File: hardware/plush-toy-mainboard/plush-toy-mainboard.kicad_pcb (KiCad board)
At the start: 4 copper layers, 90 x 60 mm, 108 parts, among them U1 ESP32-S3-WROOM-1-N16R8

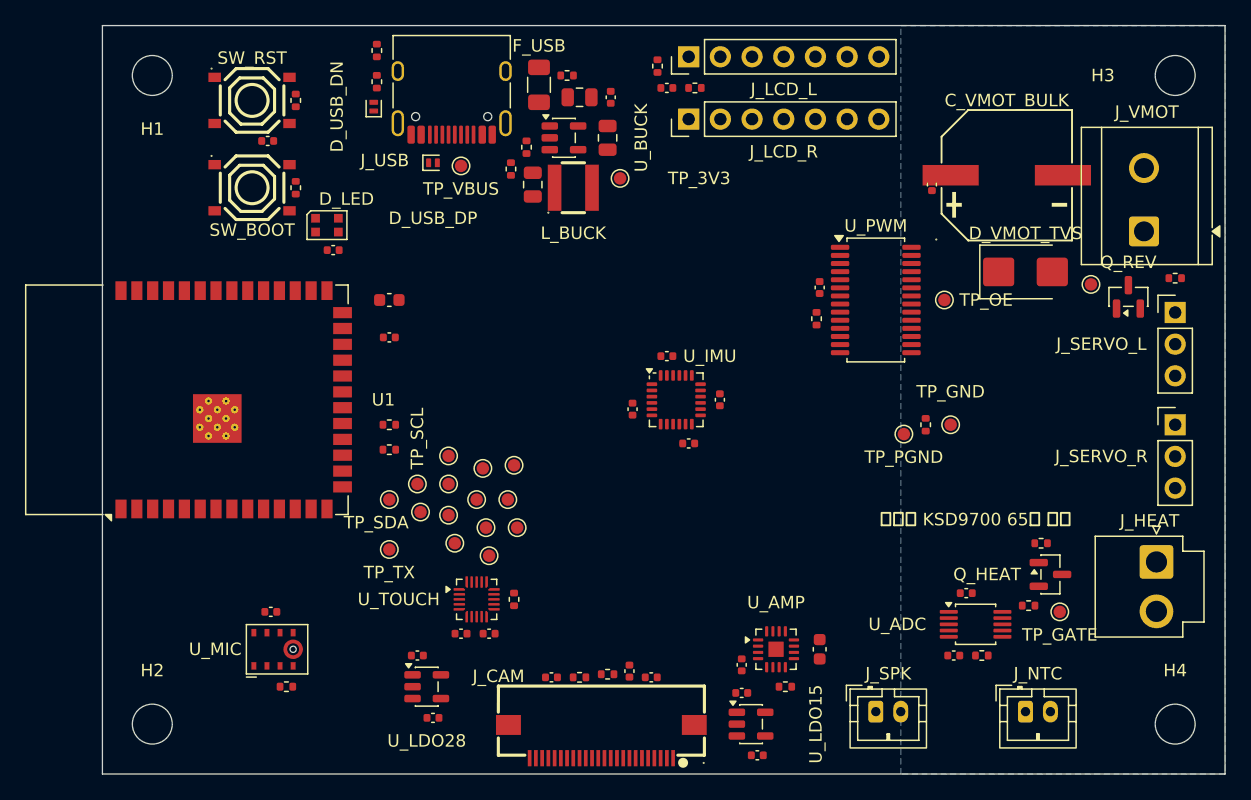
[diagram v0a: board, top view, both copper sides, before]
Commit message: fix(pcb): 布线前 DRC 清零：焊盘短路、铺铜规则、声孔间距
主板实施计划 Task 6 前半。布线前 DRC 零违规，仅剩 251 条待布线连接。

- 焊盘短路：第三方电解电容封装庭院层（±5.2mm）比焊盘（±6.75mm）小，
  自动排布把 C_VMOT_HF 的 PGND 焊盘压在 C_VMOT_BULK 的 VMOT 焊盘上。
  占位改为庭院层 ∪ 焊盘；新增 test_pads_of_different_parts_do_not_touch
- 工程规则：project_rules.py 写入网络类（Default 0.2mm、Supply 0.5mm、
  Power 1.0mm）与最小规则（线宽/间距 0.127、钻孔 0.2、距板边 0.3）
- 铺铜：临时板无工程文件，按默认规则灌铜导致 15 处孔间距、3 处板边间距违规。
  改为加载正式工程后再灌铜
- 板文件安全：生成先写临时文件再替换；此前一次报错清空了正式板文件
- INMP441 声孔 0.5 改 0.4mm：原孔到铜环 0.23mm 低于规则 0.25mm，
  0.4 仍远大于数据手册下限 0.25mm
- 新增 route.py（DSN → Freerouting → SES）与 test_drc.py

Co-Authored-By: Claude Opus 5 <noreply@anthropic.com>
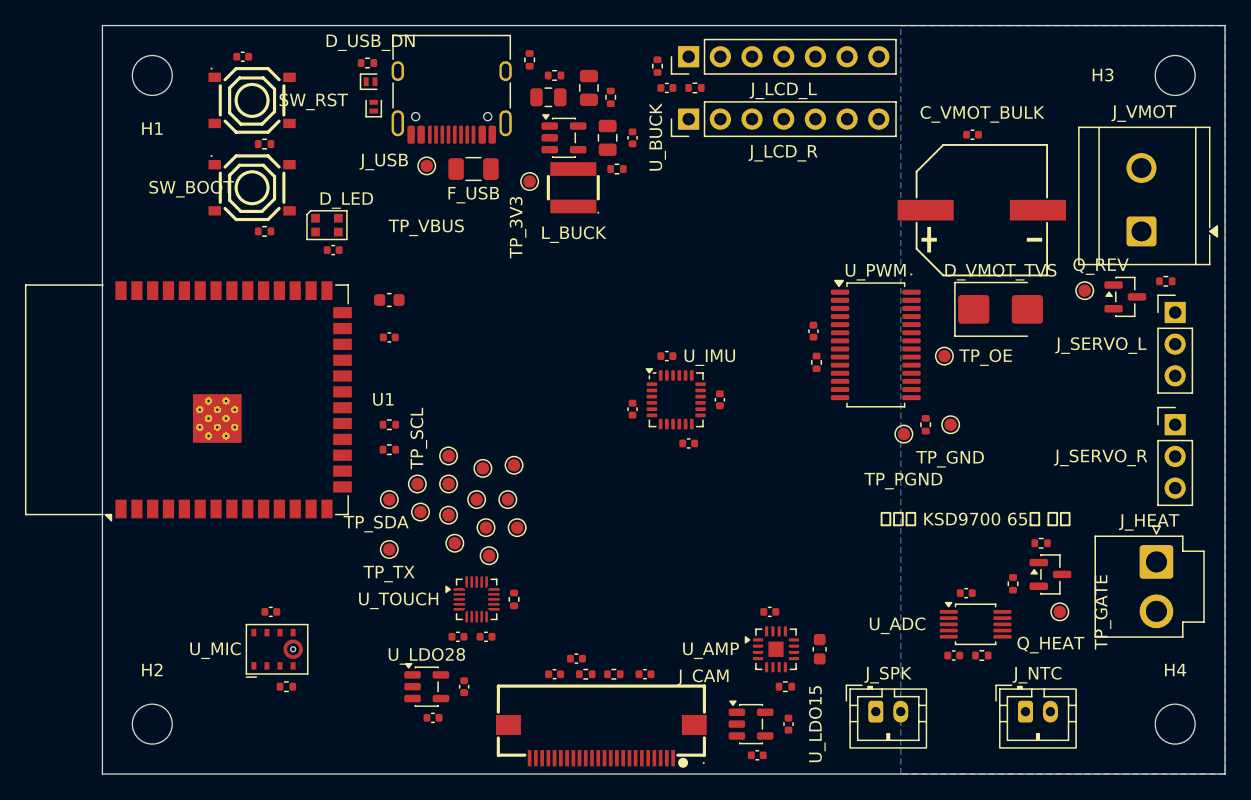
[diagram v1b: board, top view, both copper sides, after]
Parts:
- moved R_CC1 12.4 mm to (34.2, 2.75)
- moved C_BUCK_OUT2 8.96 mm to (39.0, 5.00)
- moved F_USB 8.55 mm to (29.8, 11.5), turned to 0 degrees
- moved R_FB1 8.28 mm to (36.2, 4.00), turned to 0 degrees
- moved C_CAM_AVDD 7.50 mm to (43.5, 52.0)
- moved R_BUCK_EN 7.46 mm to (41.2, 11.5), turned to 0 degrees
- moved TP_3V3 7.25 mm to (34.2, 12.5)
- moved C_EN 7.04 mm to (11.2, 2.50)
- moved D_USB_DP 6.54 mm to (21.8, 6.50), turned to 90 degrees
- moved C_CAM_DVDD 6.18 mm to (38.0, 50.8)
- moved C_CAM_RST 6.01 mm to (36.2, 52.0), turned to 0 degrees
- moved C_VMOT_HF 5.15 mm to (69.8, 8.75), turned to 0 degrees
- moved C_AMP 4.81 mm to (53.5, 47.0), turned to 0 degrees
- moved C_LDO15_OUT 4.51 mm to (55.0, 56.0), turned to 90 degrees
- moved C_LDO28_OUT 4.51 mm to (29.0, 53.0), turned to 90 degrees
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
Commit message: wip(pcb): 自动布线存档——平面扇出 + Freerouting，剩 10 条未连接
主板实施计划 Task 6 进行中，委托方要求在此存档。

- 内层 In1/In2 设为 power 类型：首次布线把 MIC、I2S 线走在了 GND/3V3 平面上
- gen_pcb / route 保存后重写工程规则：board.Save 会用默认规则冲掉 .kicad_pro，
  导致 DRC 按 0.2mm 间距报 370 处假违规
- fanout.py：GND/+3V3 贴片焊盘就近打过孔下平面（101 个），散热焊盘内打孔，
  细间距引脚按 0.15mm 规则间距外扩
- 新增测试：内层无走线、内层为 power 类型、平面网络焊盘均已扇出
- export_fab.sh：Gerber/钻孔/BOM/坐标导出，参数已对照 kicad-cli 10.0.6 帮助核对

当前结果：test_pcb 16 项全绿，与原理图一致；DRC 剩 10 条未连接、
4 处路由器过孔离 U_MIC 声孔过近（0.13mm < 0.25mm）。剩余问题清单见 README。

Co-Authored-By: Claude Opus 5 <noreply@anthropic.com>
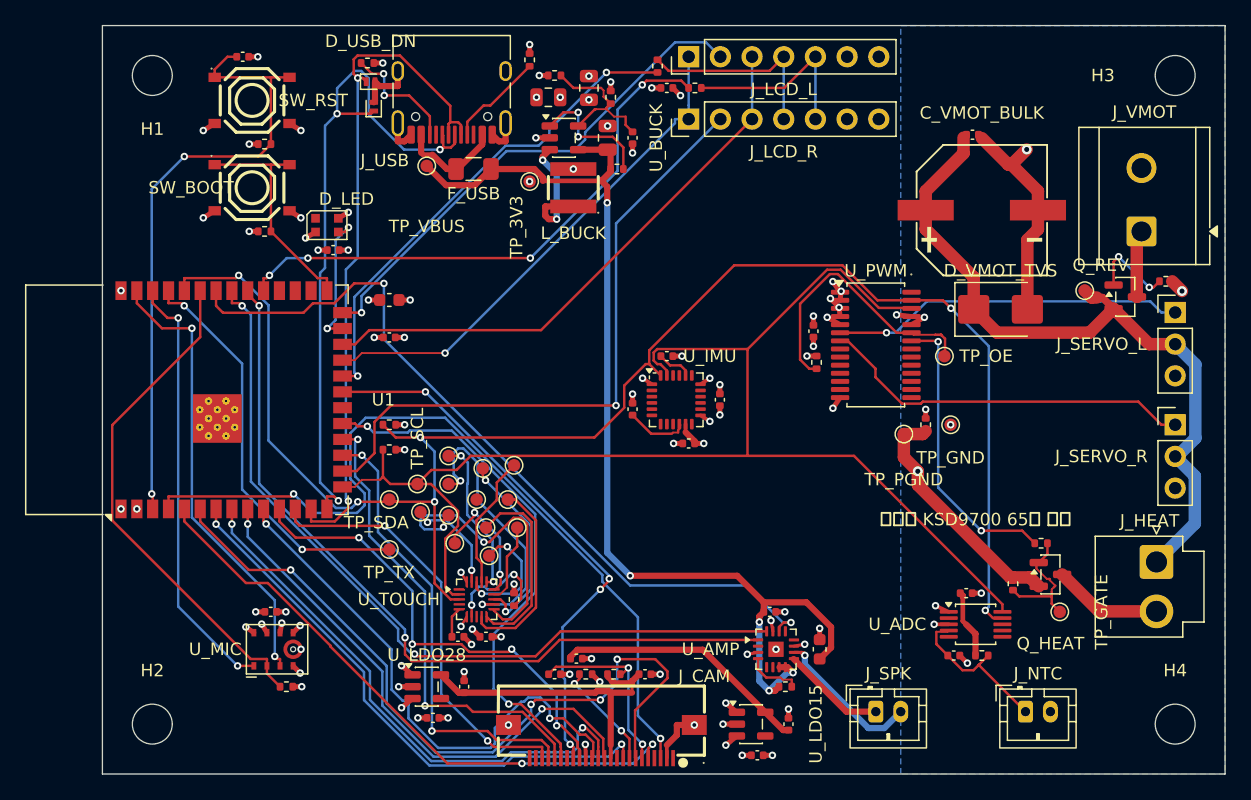
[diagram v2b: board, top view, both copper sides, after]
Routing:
- net I2C_SDA: track 0.00 -> 134.1 mm, vias 0 -> 6
- net I2C_SCL: track 0.00 -> 109.9 mm
- net VBUS: track 0.00 -> 86.7 mm, vias 0 -> 5
- net GND: track 0.00 -> 69.5 mm, vias 0 -> 70
- net CAM_SIOD: track 0.00 -> 66.5 mm, vias 0 -> 2
- net AMP_BCLK: track 0.00 -> 64.8 mm, vias 0 -> 2
- net AMP_LRCLK: track 0.00 -> 63.8 mm, vias 0 -> 2
- net AMP_DIN: track 0.00 -> 63.6 mm, vias 0 -> 2
- net CAM_VSYNC: track 0.00 -> 61.0 mm, vias 0 -> 4
- net VMOT: track 0.00 -> 59.5 mm
- net USB_DP: track 0.00 -> 55.6 mm, vias 0 -> 3
- net USB_DN: track 0.00 -> 55.4 mm, vias 0 -> 2
- net LCD_CS_R: track 0.00 -> 52.0 mm, vias 0 -> 1
- net EN: track 0.00 -> 51.0 mm, vias 0 -> 2
- net CAM_SIOC: track 0.00 -> 48.5 mm, vias 0 -> 2
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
